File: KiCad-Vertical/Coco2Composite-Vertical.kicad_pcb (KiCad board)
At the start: 2 copper layers, 65.1 x 39.7 mm, 20 parts, among them J1 TO_COCO2, J2 AUDIO_JACK_3.5MM_KIT, Q1 PN2907, Q2 2N2222, U1 MC1372

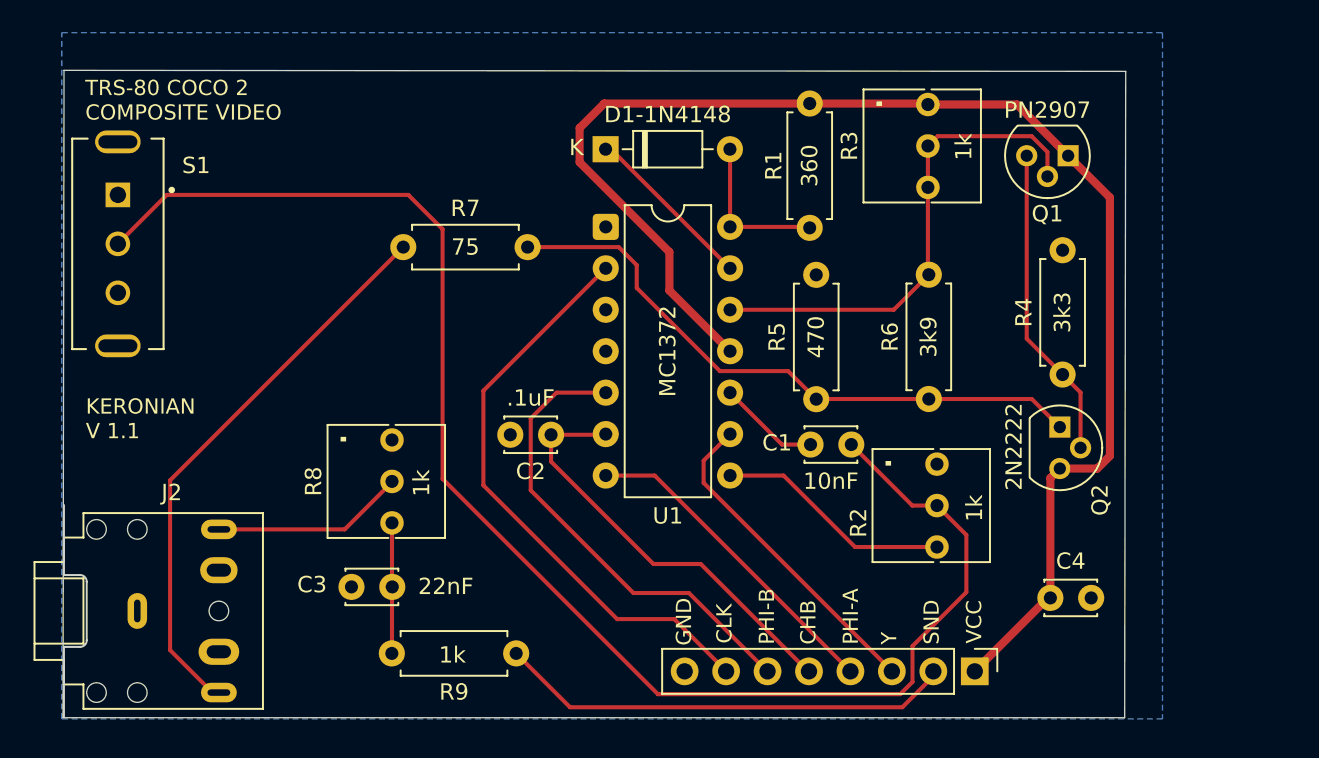
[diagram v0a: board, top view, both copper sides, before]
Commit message: Fixed associations and made cap value visible for vert board
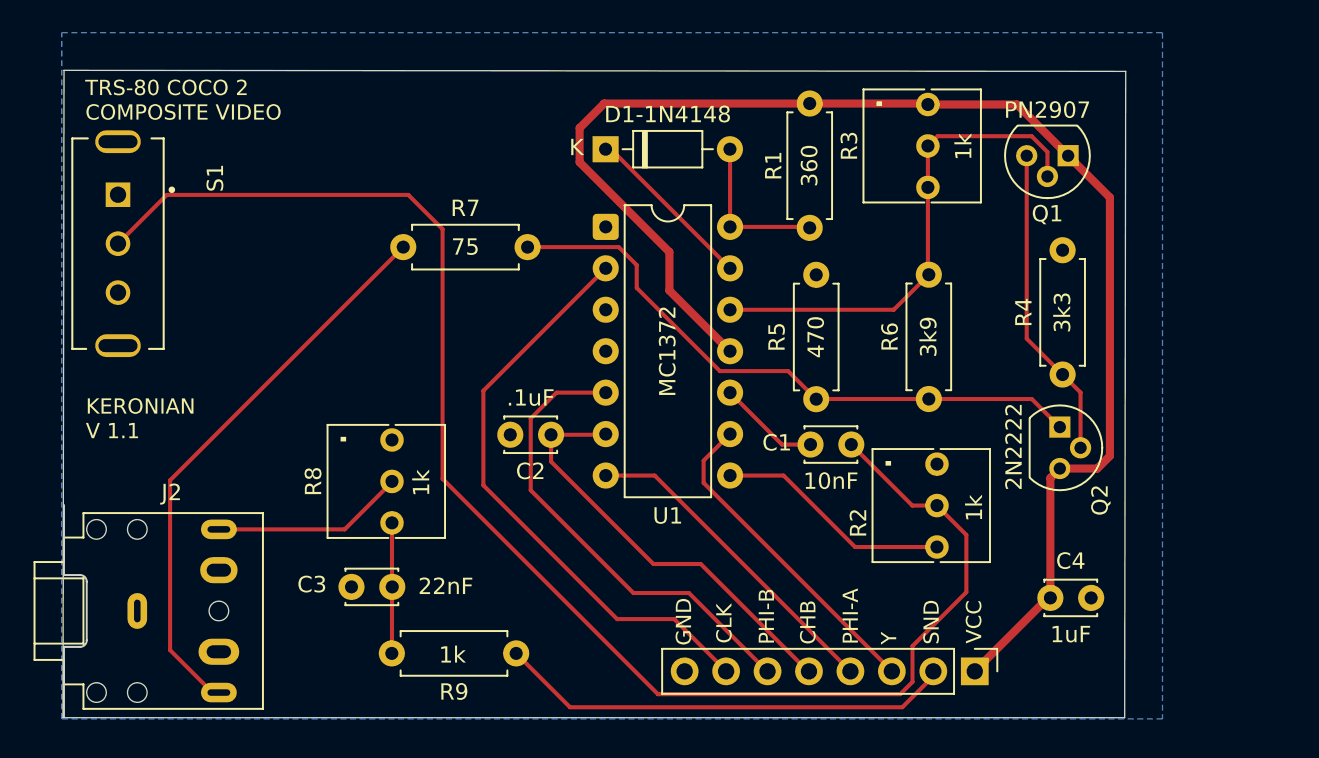
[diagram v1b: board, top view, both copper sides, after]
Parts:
- S1: value SW_SLW-1298856-5A-RA-N-D -> SLW-1298856-5A-RA-N-D
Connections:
- S1 pad 1: (no net) -> unconnected-(S1-Pad1)

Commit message: Added supports for vertical board
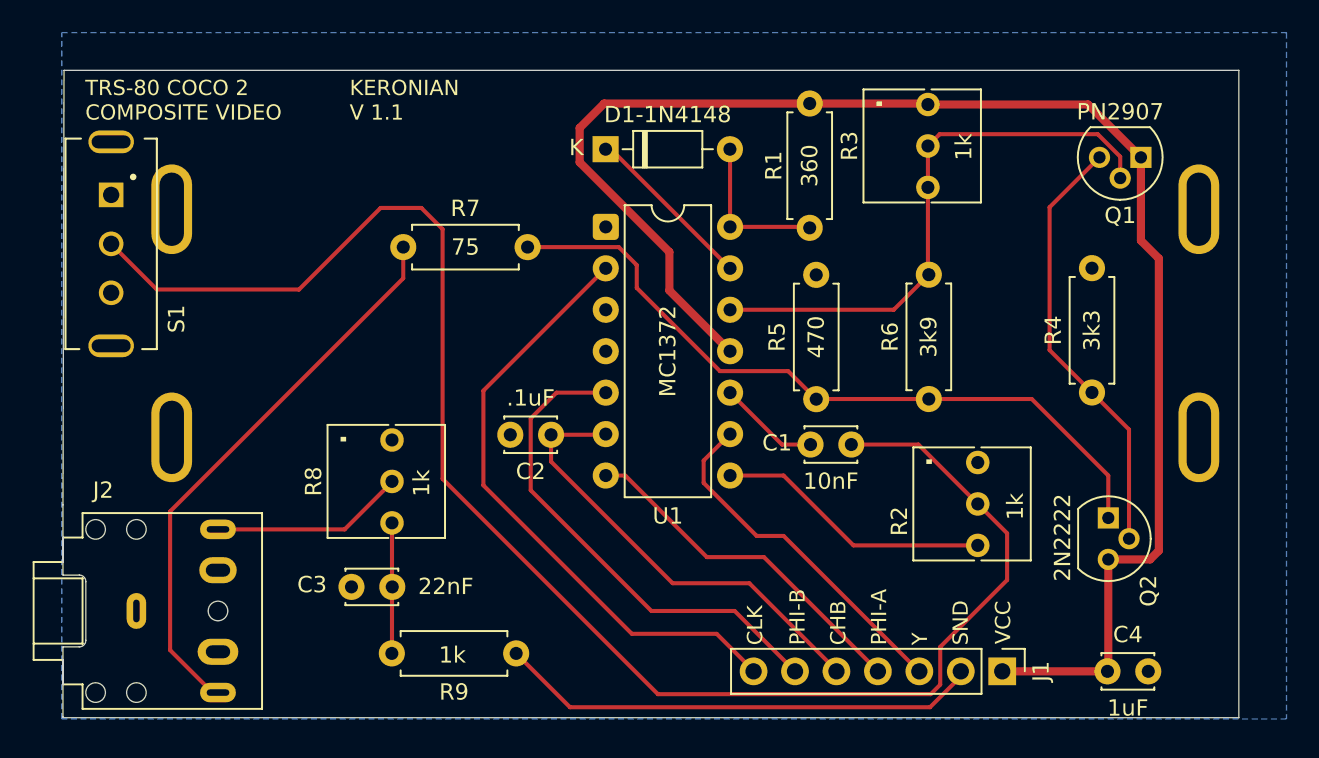
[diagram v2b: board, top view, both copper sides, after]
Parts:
- added ?: , , F.Cu at (185.6, 107.7)
- added ?: , , F.Cu at (122.6, 107.7)
- added REF**: MountingSlot, Custom:MountingSlot, F.Cu at (181.6, 99.7)
- added REF**: MountingSlot, Custom:MountingSlot, F.Cu at (118.1, 93.5)
- J1: footprint Connector_PinHeader_2.54mm:PinHeader_1x08_P2.54mm_Vertical -> Connector_PinHeader_2.54mm:PinHeader_1x07_P2.54mm_Vertical
- moved Q2 6.31 mm to (180.0, 112.6)
- moved C4 5.70 mm to (179.9, 122.0)
- moved Q1 4.46 mm to (182.0, 90.5)
- moved R2 2.50 mm to (172.0, 109.2)
- moved R4 2.11 mm to (179.0, 104.9)
- moved J1 1.68 mm to (173.5, 122.0)
- moved S1 0.42 mm to (118.9, 95.8)
- moved J2 0.05 mm to (120.4, 118.3)
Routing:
- net VCC: track 87.1 -> 95.1 mm
- net Net-(Q2-B): track 19.3 -> 26.7 mm
- net Net-(C1-Pad2): track 91.6 -> 98.4 mm
- net Net-(Q2-E): track 38.1 -> 44.8 mm
- net Net-(U1-RF_OUT): track 30.5 -> 34.9 mm
- net Net-(U1-CHROM_MOD_OUT): track 14.5 -> 17.0 mm
- net /SND: track 27.7 -> 29.7 mm
- net /CLK: track 36.0 -> 37.7 mm
- net /CHB: track 26.2 -> 27.9 mm
- net /PHI-A: track 20.0 -> 21.7 mm
- net /PHI-B: track 28.8 -> 30.5 mm
- net /Y: track 20.0 -> 21.6 mm
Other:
- board size 65.1 x 39.7 mm -> 72.1 x 39.7 mm
- board text removed: "GND"
